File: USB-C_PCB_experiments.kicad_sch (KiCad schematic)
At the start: 0 parts

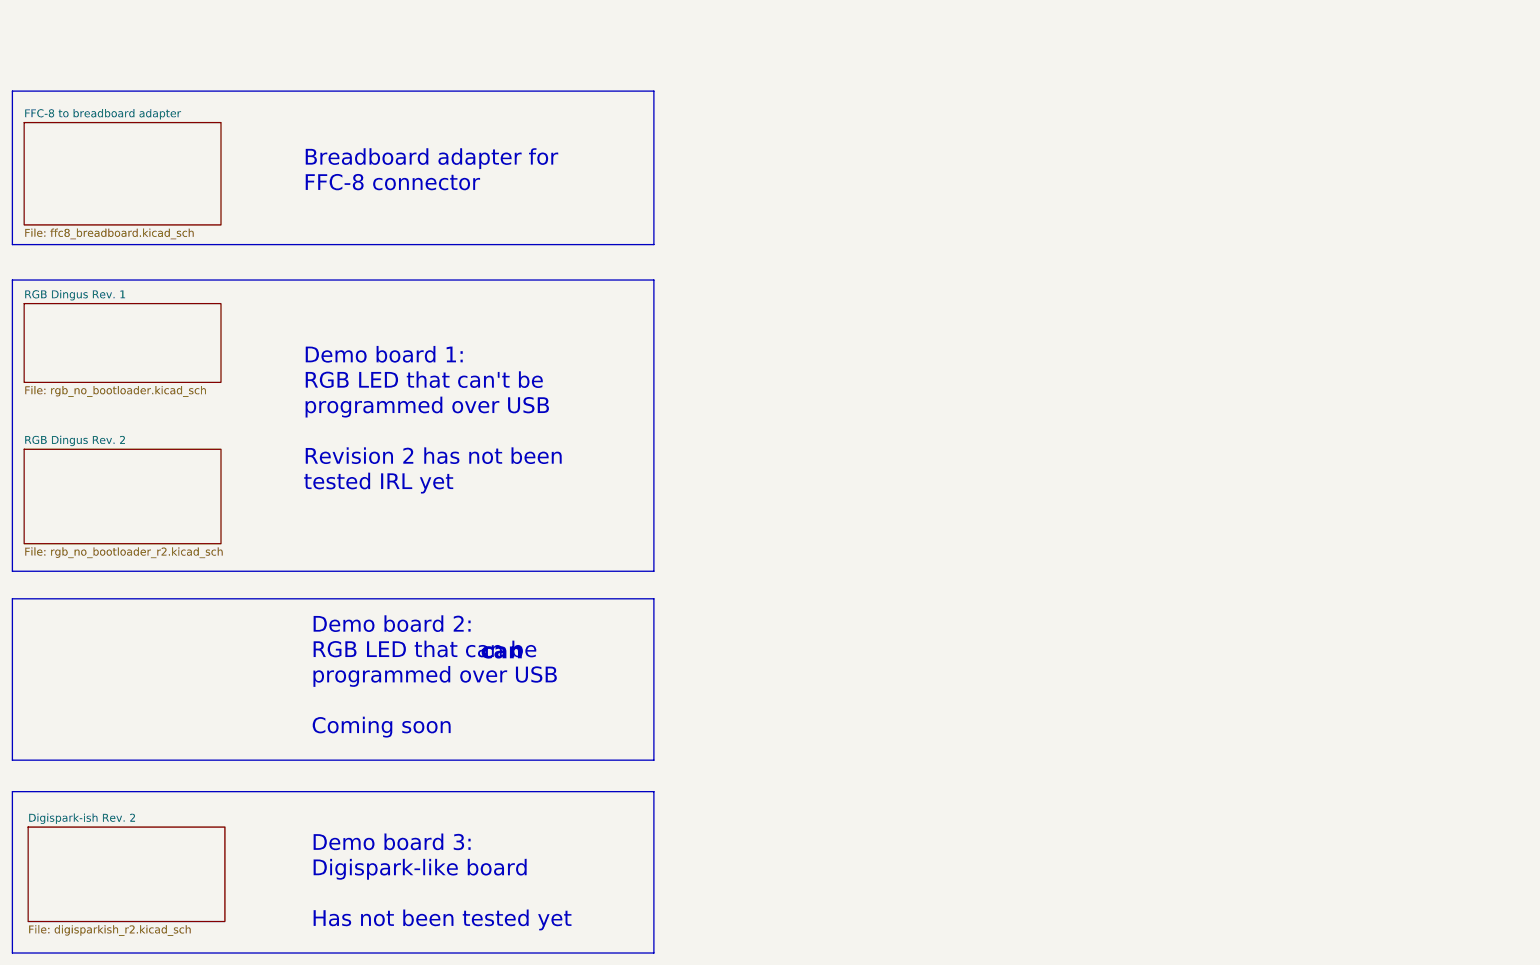
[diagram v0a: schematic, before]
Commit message: Finished routing Demo 2, added Demo 4, updated readme with newer findings
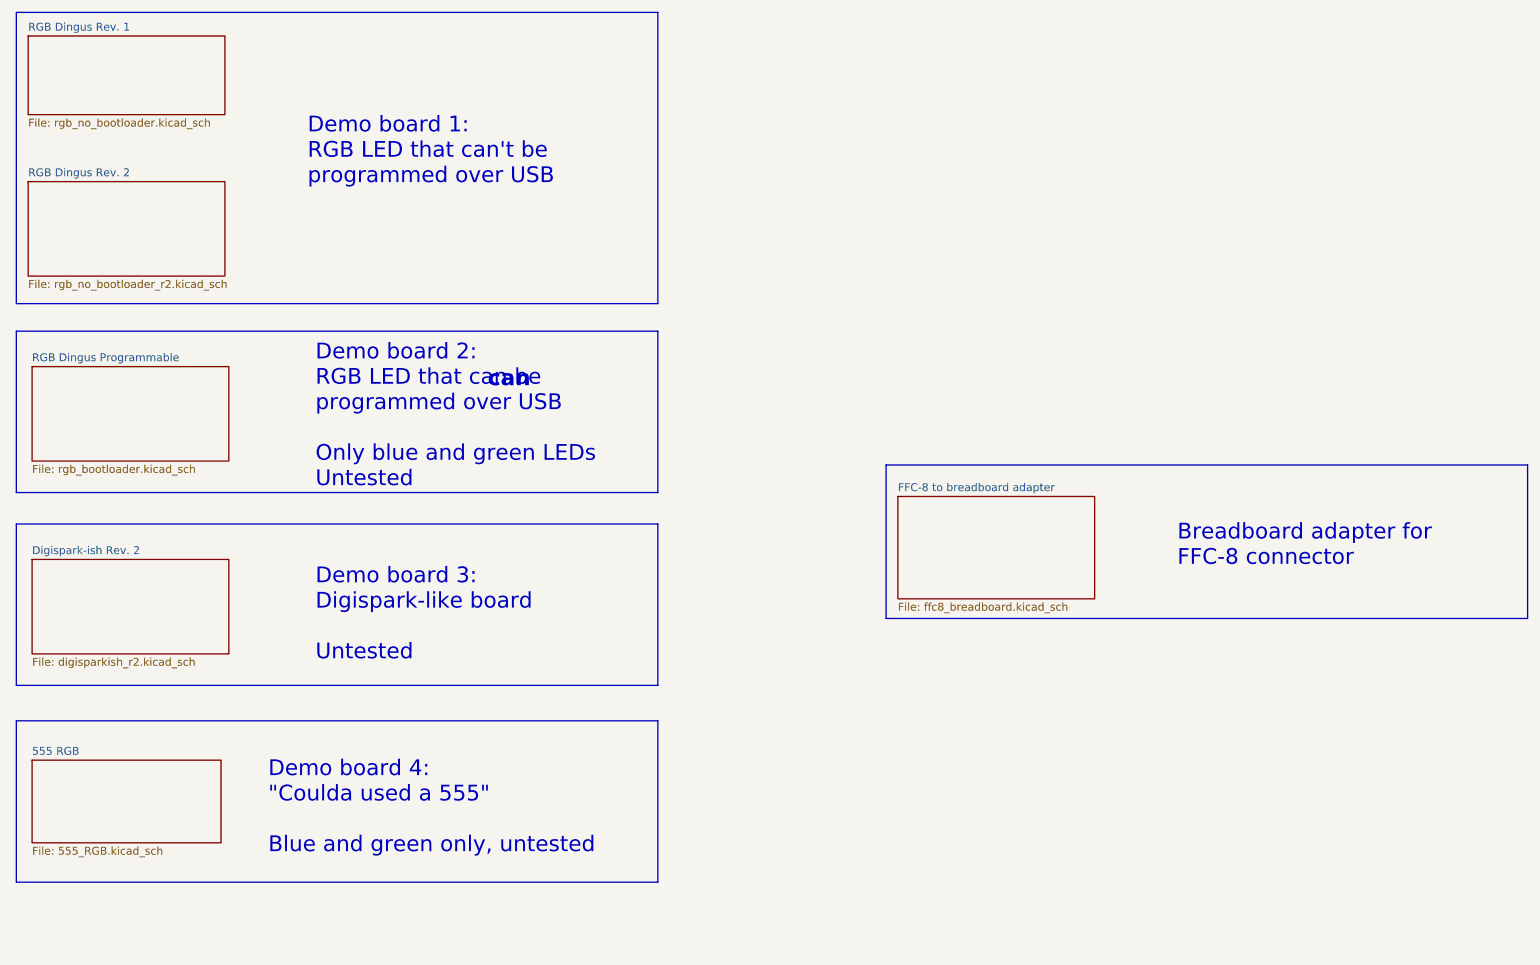
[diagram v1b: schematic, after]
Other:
- added sheet 555 RGB (555_RGB.kicad_sch)
- added sheet RGB Dingus Programmable (rgb_bootloader.kicad_sch)
- note added: "Demo board 1: RGB LED that can't be programmed over USB"
- note added: "Demo board 2: RGB LED that can be programmed over USB Only blue and green LEDs Untested"
- note added: "Demo board 3: Digispark-like board Untested"
- note added: "Demo board 4: "Coulda used a 555" Blue and green only, untested"
- note removed: "Demo board 1: RGB LED that can't be programmed over USB Revision 2 has not been tested IRL yet"
- note removed: "Demo board 2: RGB LED that can be programmed over USB Coming soon"
- note removed: "Demo board 3: Digispark-like board Has not been tested yet"
